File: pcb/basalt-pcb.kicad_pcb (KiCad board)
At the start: 2 copper layers, 29 x 42 mm, 12 parts, among them J1 Conn_01x07_Pin, J2 Conn_01x07_Pin, J3 USB4215-03-A, J4 Conn_01x04_Pin, U1 DI78L3.3ZAB, U2 STM32C071F8Px

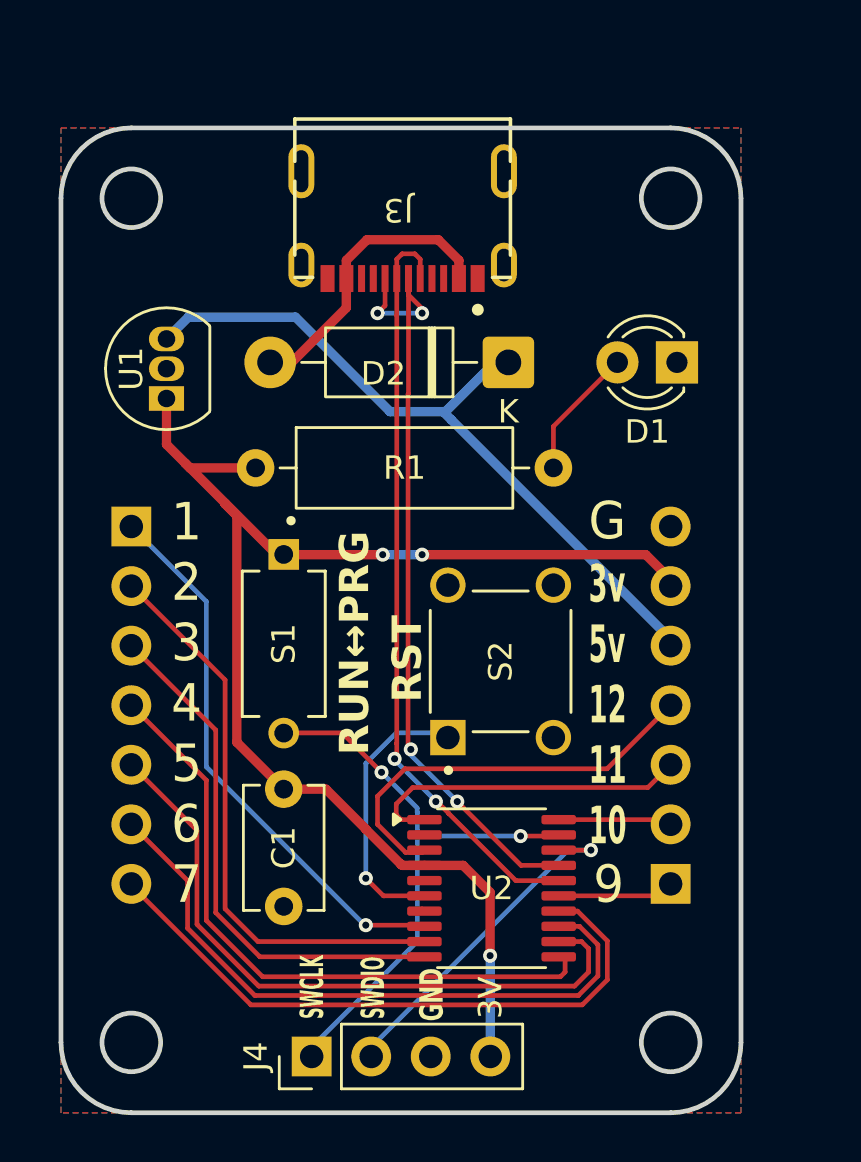
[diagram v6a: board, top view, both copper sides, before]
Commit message: Fix mounting holes
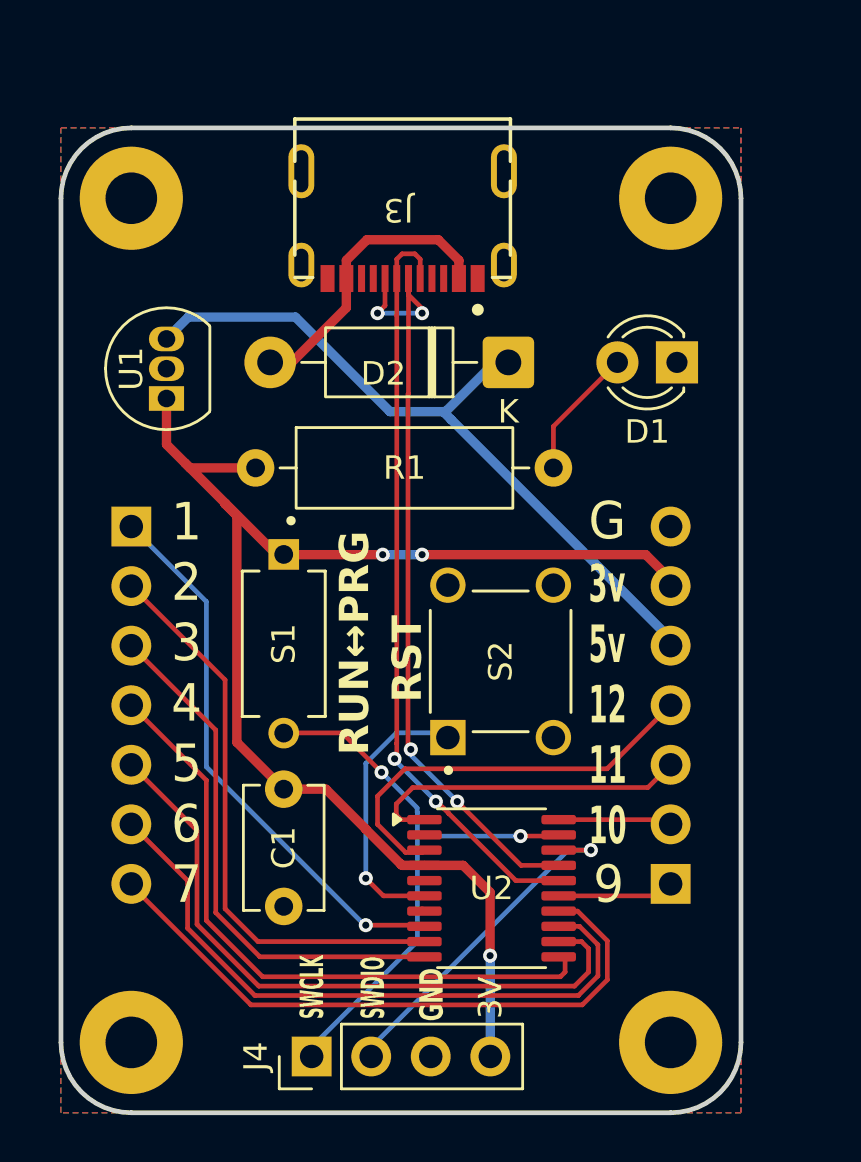
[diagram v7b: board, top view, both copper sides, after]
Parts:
- added H1: MountingHole_Pad, MountingHole:MountingHole_2.2mm_M2_Pad, F.Cu at (135.0, 83.0)
- added H2: MountingHole_Pad, MountingHole:MountingHole_2.2mm_M2_Pad, F.Cu at (158.0, 83.0)
- added H3: MountingHole_Pad, MountingHole:MountingHole_2.2mm_M2_Pad, F.Cu at (135.0, 119.0)
- added H4: MountingHole_Pad, MountingHole:MountingHole_2.2mm_M2_Pad, F.Cu at (158.0, 119.0)
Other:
- outline, holes or cut-outs redrawn
